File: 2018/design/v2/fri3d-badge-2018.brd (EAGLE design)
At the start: 80 x 60 mm, 1 part

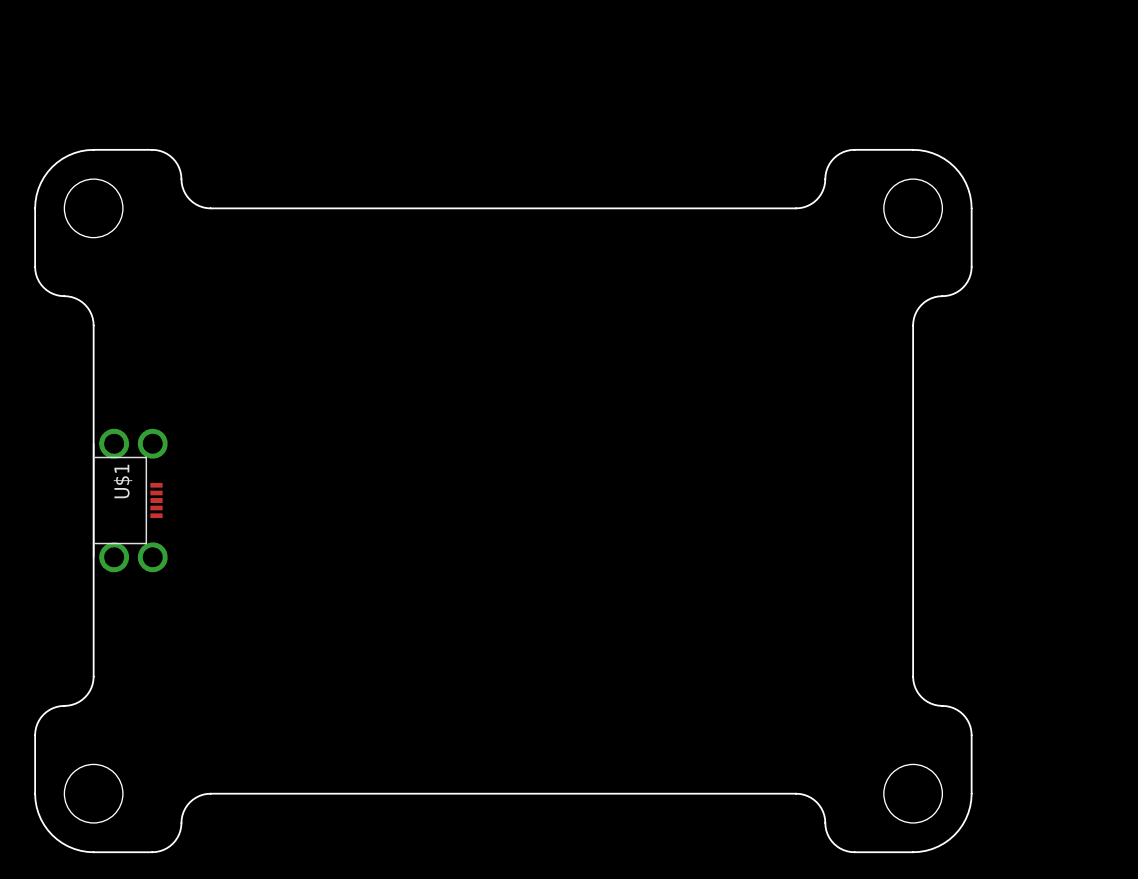
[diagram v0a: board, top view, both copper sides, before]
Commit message: completed draft of schematic for prototype 2
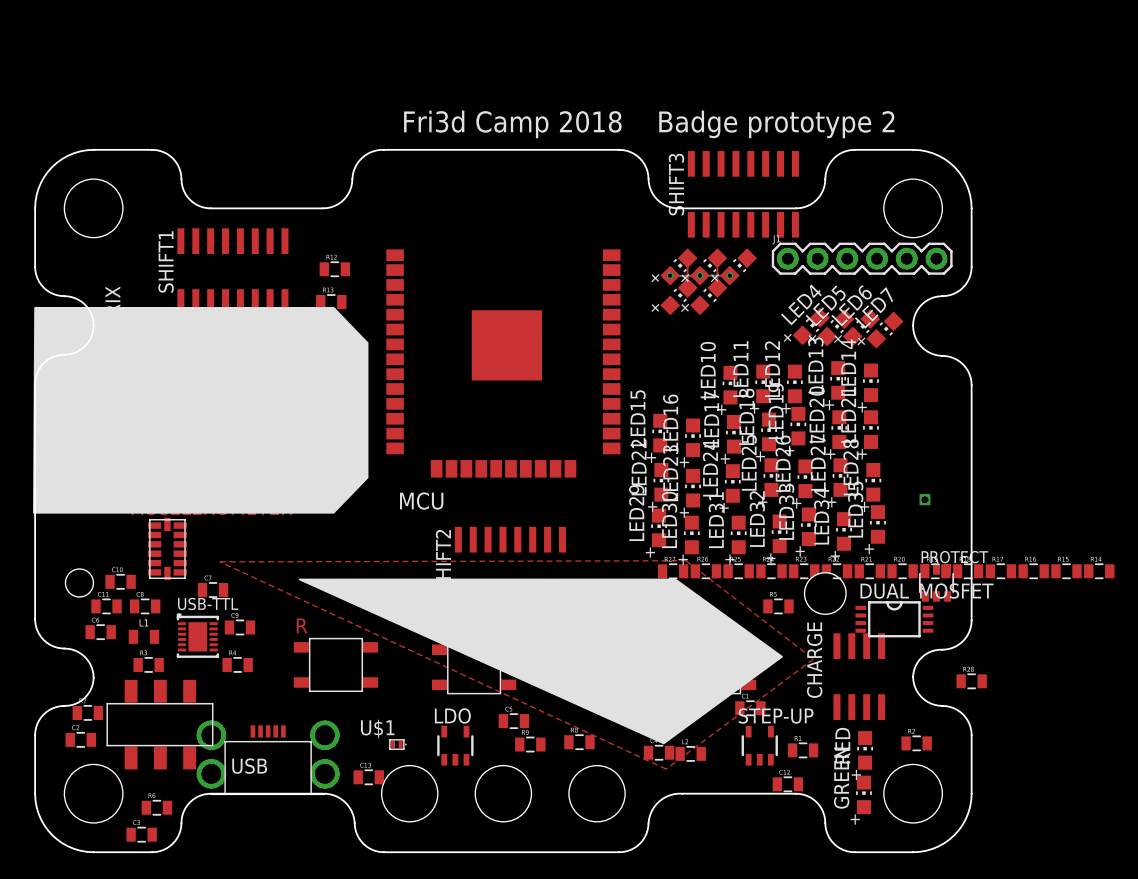
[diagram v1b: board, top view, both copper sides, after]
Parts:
- added A, B, D, R: SWITCH-MOMENTARY-4.5MM, switches:SWITCH-MOMENTARY-4.5MM
- added ACCELEROMETER: ADXL345BCCZ, ic:LGA
- added C1, C2: 10uF, passive:0805
- added C10: 4.7uF, passive:0805
- added C11, C3, C9: 0.1uF, passive:0805
- added C12, C13: 22uF, passive:0805
- added C4, C5: 1uF, passive:0805
- added C6, C7: 47pF, passive:0805
- added C8: 0.01uF, passive:0805
- added CHARGE: TP4056, power:SO8
- added DUAL_MOSFET: FS8205A, ic:TSSOP8
- added GREEN, LED1, LED10, LED11, LED12, LED13, LED14, LED15, LED16, LED17, LED18, LED19, LED2, LED20, LED21, LED22, LED23, LED24, LED25, LED26, LED27, LED28, LED29, LED3, LED30, LED31, LED32, LED33, LED34, LED35, LED4, LED5, LED6, LED7, LED8, LED9, RED: (no value), led:CHIP-LED0805
- added J1: (no value), SparkFun-Connectors:1X06
- added L1: (no value), SparkFun-Coils:0805
- added L2: 10uH, passive:0805
- added LDO: XC6210, power:SOT23-5
- added MCU: ESP-WROOM-32, esp32:ESP-WROOM-32
- added PROTECT: DW01-P, power:SOT23-6
- added R1, R2, R7: 1K, passive:0805
- added R10, R11, R8, R9: 10K, passive:0805
- added R12: 82K, passive:0805
- added R13: 11K, passive:0805
- added R14, R15, R16, R17, R18, R19, R20, R21, R22, R23, R24, R25, R26, R27: (no value), passive:0805
- added R28: 0, passive:0805
- added R3, R4: 27, passive:0805
- added R5: 1.2K, passive:0805
- added R6: 100, passive:0805
- added RIGHT_EYE: 5x7 LED DOT MATRIX, led:5X7_DOT_LED_MATRIX
- added SHIFT1, SHIFT2, SHIFT3: 74HC595, ic:SO16
- added STEP-UP: SX1308, power:SOT23-5
- added U$3: CR18650, setup:BATTERY_HOLDER_18650
- added U$7: SLIDE_DPDT, switches:SLIDE_SWITCH
- added USB: USB_MICRO_B, connector:USB_MICRO_B
- added USB-TTL: FT234XD, ftdi-chip:DFN12
- U$1: value USB_MICRO_B -> SCHOTTKY; device connector:USB_MICRO_B -> passive:SOD993
- moved U$1 29.3 mm to (30.9, 9.20), turned to 0 degrees
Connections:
- new net 3V3: A.P$3, A.P$4, ACCELEROMETER.1, ACCELEROMETER.6, B.P$3, B.P$4, C5.1, LDO.5, MCU.2, R8.2, R9.2, SHIFT1.10, SHIFT1.16, SHIFT2.10, SHIFT2.16, SHIFT3.10, SHIFT3.16
- new net 5V: U$7.P$5
- new net 5V_ENABLE: STEP-UP.4
- new net ACC_ENABLE: ACCELEROMETER.7
- new net ACC_INT1: ACCELEROMETER.8
- new net ACC_INT2: ACCELEROMETER.9
- new net ACC_MISO: ACCELEROMETER.12
- new net ACC_MOSI: ACCELEROMETER.13
- new net ACC_SCK: ACCELEROMETER.14
- new net BUTTON-A: B.P$1, B.P$2, R10.2
- new net BUTTON-B: A.P$1, A.P$2, R11.2
- new net D+: C6.1, R4.1, USB.D+
- new net D-: C7.1, R3.1, USB.D-
- new net DOWNLOAD: D.P$1, D.P$2, MCU.25, R9.1
- new net GND: ACCELEROMETER.2, ACCELEROMETER.4, ACCELEROMETER.5, C1.2, C10.2, C11.2, C12.2, C13.2, C2.2, C4.2, C5.2, C6.2, C7.2, C8.2, C9.2, CHARGE.1, CHARGE.3, D.P$3, D.P$4, DUAL_MOSFET.6, DUAL_MOSFET.7, J1.1, LDO.2, MCU.1, MCU.15, MCU.38, MCU.GND, R.P$3, R.P$4, R10.1, R11.1, R13.1, R28.1, R5.1, R7.2, SHIFT1.8, SHIFT2.8, SHIFT3.8, STEP-UP.2, USB-TTL.13, USB-TTL.5, USB.GND, USB.P$6, USB.P$7, USB.P$8, USB.P$9
- new net LC1: R14.1
- new net LC2: R15.1
- new net LC3: R16.1
- new net LC4: R17.1
- new net LC5: R18.1
- new net LC6: R19.1
- new net LC7: R20.1
- new net LEDS_ENABLE: SHIFT1.13, SHIFT2.13, SHIFT3.13
- new net LEDS_RCK: SHIFT1.12, SHIFT2.12, SHIFT3.12
- new net LEDS_SCK: SHIFT1.11, SHIFT2.11, SHIFT3.11
- new net LEDS_SIN: SHIFT1.14
- new net LR1: LED1.A, LED2.A, LED3.A, LED4.A, LED5.A, LED6.A, LED7.A
- new net LR2: LED10.A, LED11.A, LED12.A, LED13.A, LED14.A, LED8.A, LED9.A
- new net LR3: LED15.A, LED16.A, LED17.A, LED18.A, LED19.A, LED20.A, LED21.A
- new net LR4: LED22.A, LED23.A, LED24.A, LED25.A, LED26.A, LED27.A, LED28.A
- new net LR5: LED29.A, LED30.A, LED31.A, LED32.A, LED33.A, LED34.A, LED35.A
- new net N$10: CHARGE.2, R5.2
- new net N$11: C3.2, DUAL_MOSFET.2, DUAL_MOSFET.3, PROTECT.6, R28.2, U$3.-
- new net N$12: PROTECT.2, R7.1
- new net N$13: C3.1, PROTECT.5, R6.2
- new net N$14: DUAL_MOSFET.4, PROTECT.1
- new net N$15: DUAL_MOSFET.5, PROTECT.3
- new net N$18: R12.1, R13.2, STEP-UP.3
- new net N$19: L2.2, STEP-UP.1, U$1.P$1
- new net N$20: SHIFT1.9, SHIFT2.14
- new net N$21: SHIFT2.9, SHIFT3.14
- new net N$22: SHIFT1.7
- new net N$23: SHIFT1.6
- new net N$24: SHIFT1.5
- new net N$25: SHIFT1.4
- new net N$26: SHIFT1.15
- new net N$27: SHIFT1.1
- new net N$28: SHIFT1.2
- new net N$29: SHIFT1.3
- new net N$3: R3.2, USB-TTL.1
- new net N$30: R21.1, RIGHT_EYE.11
- new net N$31: R22.1, RIGHT_EYE.12
- new net N$32: LED1.C, LED15.C, LED22.C, LED29.C, LED8.C, R14.2
- new net N$33: LED16.C, LED2.C, LED23.C, LED30.C, LED9.C, R15.2
- new net N$34: LED10.C, LED17.C, LED24.C, LED3.C, LED31.C, R16.2
- new net N$35: LED11.C, LED18.C, LED25.C, LED32.C, LED4.C, R17.2
- new net N$36: LED12.C, LED19.C, LED26.C, LED33.C, LED5.C, R18.2
- new net N$37: LED13.C, LED20.C, LED27.C, LED34.C, LED6.C, R19.2
- new net N$38: LED14.C, LED21.C, LED28.C, LED35.C, LED7.C, R20.2
- new net N$39: R24.1, RIGHT_EYE.9
- new net N$4: CHARGE.7, R1.1
- new net N$40: R23.1, RIGHT_EYE.2
- new net N$41: R25.1, RIGHT_EYE.4
- new net N$42: R26.1, RIGHT_EYE.5
- new net N$43: R27.1, RIGHT_EYE.6
- new net N$44: SHIFT2.7
- new net N$45: SHIFT2.6
- new net N$46: SHIFT2.5
- new net N$47: SHIFT2.4
- new net N$48: SHIFT2.15
- new net N$49: SHIFT2.1
- new net N$5: R4.2, USB-TTL.12
- new net N$50: SHIFT2.2
- new net N$51: SHIFT2.3
- new net N$52: SHIFT3.7
- new net N$53: SHIFT3.6
- new net N$54: SHIFT3.5
- new net N$55: SHIFT3.4
- new net N$56: SHIFT3.15
- new net N$57: SHIFT3.1
- new net N$58: SHIFT3.2
- new net N$59: SHIFT3.3
- new net N$6: C9.1, USB-TTL.2, USB-TTL.3, USB-TTL.9
- new net N$7: CHARGE.6, R2.1
- new net N$8: R1.2, RED.C
- new net N$9: GREEN.C, R2.2
- new net RC1: R21.2
- new net RC2: R22.2
- new net RC3: R23.2
- new net RC4: R24.2
- new net RC5: R25.2
- new net RC6: R26.2
- new net RC7: R27.2
- new net RESET: MCU.3, R.P$1, R.P$2, R8.1
- new net RR1: RIGHT_EYE.1
- new net RR2: RIGHT_EYE.3
- new net RR3: RIGHT_EYE.10
- new net RR4: RIGHT_EYE.7
- new net RR5: RIGHT_EYE.8
- new net RX: J1.4, MCU.34, USB-TTL.7
- new net TX: J1.5, MCU.35, USB-TTL.10
- new net USB-RAW: C8.1, L1.1, USB.VBUS
- new net VBAT: C1.1, CHARGE.5, R6.1, U$3.+, U$7.P$3
- new net VCC: C12.1, C4.1, L2.1, LDO.1, LDO.3, STEP-UP.5, U$7.P$2
- new net VSTEPUP: C13.1, R12.2, U$1.P$2, U$7.P$4
- new net VUSB: C10.1, C11.1, C2.1, CHARGE.4, CHARGE.8, GREEN.A, L1.2, RED.A, U$7.P$1, U$7.P$6, USB-TTL.4
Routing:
- net LR1: track 0.00 -> 5.11 mm, vias 0 -> 3
- net N$32: track 0.00 -> 2.56 mm
- net N$33: track 0.00 -> 2.56 mm
- added copper zone on layer 1, net N$1
- added copper zone on layer 1, net N$2
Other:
- outline, holes or cut-outs redrawn
- board text added: "Badge prototype 2"
- board text added: "Fri3d Camp 2018"

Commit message: added extension headers + expansion board
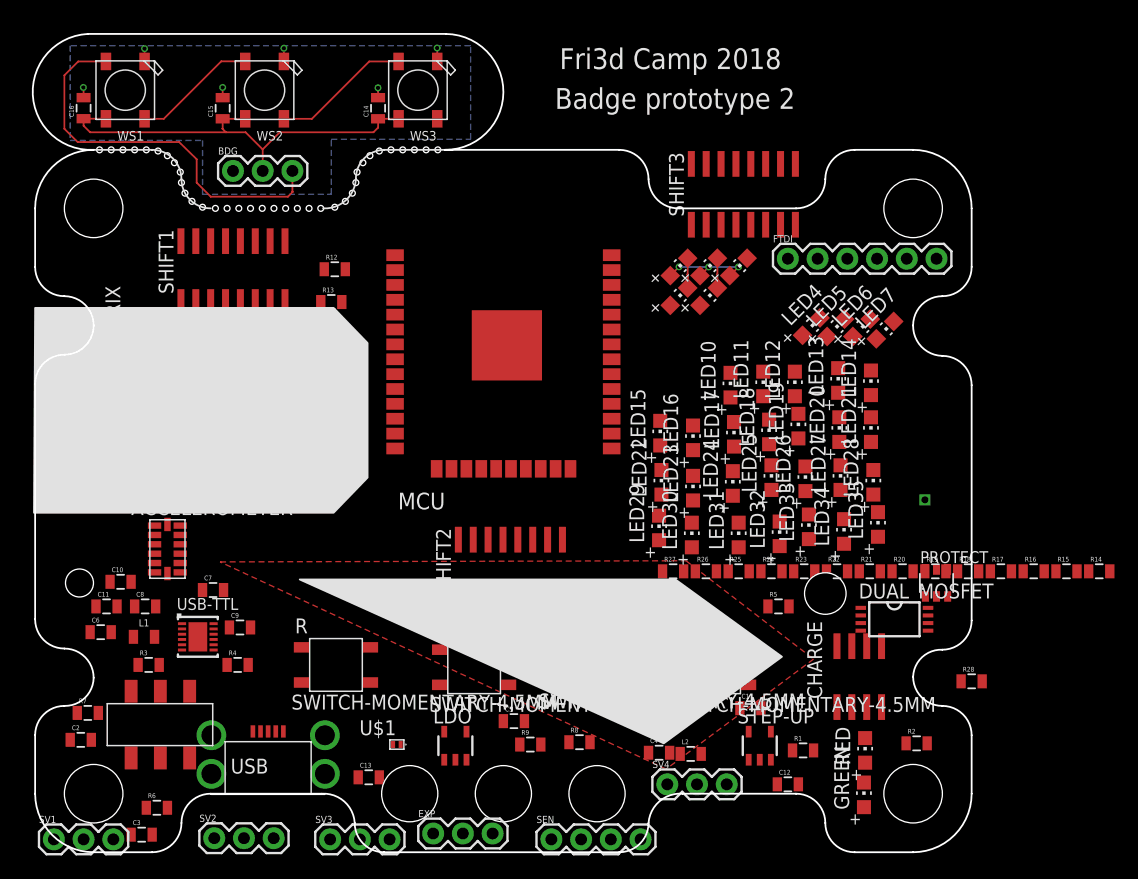
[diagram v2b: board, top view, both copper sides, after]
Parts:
- added BDG, EXP, SV1, SV2, SV3, SV4: (no value), SparkFun-Connectors:1X03
- added C14, C15, C16: 0.1uF, passive:0805
- added SEN: (no value), SparkFun-Connectors:1X04
- added WS1, WS2, WS3: WS2812B5050, adafruit:WS2812B
- renumbered J1 to FTDI, U$7 to PWR
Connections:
- new net ECHO: SEN.2
- new net EXP_3V3: BDG.2, C14.1, C15.1, C16.1, WS1.1-VDD, WS2.1-VDD, WS3.1-VDD
- new net EXP_GND: BDG.1, C14.2, C15.2, C16.2, WS1.3-GND, WS2.3-GND, WS3.3-GND
- new net EXP_IO: EXP.3
- new net N$17: WS1.2-DOUT, WS2.4-DIN
- new net N$60: WS2.2-DOUT, WS3.4-DIN
- new net N$61: BDG.3, WS1.4-DIN
- new net PULSE: SEN.3
- new net SERVO1: SV1.3
- new net SERVO2: SV2.3
- new net SERVO3: SV3.3
- new net SERVO4: SV4.3
- net 3V3: now also A.3, A.4, B.3, B.4, EXP.2; no longer A.P$3, A.P$4, B.P$3, B.P$4
- net 5V: now also SEN.4, SV1.2, SV2.2, SV3.2, SV4.2
- net BUTTON-A: now also B.1, B.2; no longer B.P$1, B.P$2
- net BUTTON-B: now also A.1, A.2; no longer A.P$1, A.P$2
- net DOWNLOAD: now also D.1, D.2; no longer D.P$1, D.P$2
- net GND: now also D.3, D.4, EXP.1, R.3, R.4, SEN.1, SV1.1, SV2.1, SV3.1, SV4.1; no longer D.P$3, D.P$4, R.P$3, R.P$4
- net RESET: now also R.1, R.2; no longer R.P$1, R.P$2
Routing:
- net EXP_3V3: track 0.00 -> 36.9 mm
- net N$61: track 0.00 -> 33.6 mm
- net N$60: track 0.00 -> 11.8 mm
- net N$17: track 0.00 -> 10.6 mm
- net EXP_GND: track 0.00 -> 5.97 mm, vias 0 -> 6
- net LR1: track 5.11 -> 8.23 mm
- added copper zone on layer 16, net EXP_GND
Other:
- board size 80 x 60 mm -> 80.2 x 69.9 mm

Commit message: completed first layout prototype 2
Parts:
- removed ACCELEROMETER: ADXL345BCCZ, ic:LGA
- added ACC: ADXL345BCCZ, ic:LGA
- added C17, C18, C19: 1uF, passive:0805
- added D1: SCHOTTKY, passive:SOD993
- added LDO_MCU: XC6210, power:SOT23-5
- added Q1: (no value), mosfet:SOT23
- added R29: 0, passive:0805
- added R30: 240, passive:0805
- added R31, R32: 10K, passive:0805
- added R33: 1K, passive:0805
- R14, R15, R16, R17, R18, R19, R20, R21, R22, R23, R24, R25, R26, R27: value (none) -> 100
- U$1: value SCHOTTKY -> KLJ-1230; device passive:SOD993 -> sound:KLJ-1230
- moved R7 71.6 mm to (72.3, 35.0)
- moved C3 68.9 mm to (73.4, 26.3)
- moved R21 67.4 mm to (5.30, 37.7), turned to 270 degrees
- moved R22 66.6 mm to (3.30, 37.7), turned to 270 degrees
- moved R6 63.1 mm to (69.4, 26.3)
- moved R23 58.1 mm to (9.27, 37.7), turned to 270 degrees
- moved R24 57.3 mm to (7.30, 37.7), turned to 270 degrees
- moved SV1 55.7 mm to (54.9, 17.3)
- moved R2 51.1 mm to (24.5, 14.8), turned to 90 degrees
- moved RED 50.0 mm to (21.7, 17.3), turned to 270 degrees
- moved CHARGE 47.1 mm to (23.6, 9.60)
- moved GREEN 46.9 mm to (25.6, 17.3), turned to 90 degrees
- moved R5 45.6 mm to (19.6, 8.62)
- moved R13 45.1 mm to (47.8, 7.90), turned to 90 degrees
- moved R12 44.5 mm to (47.8, 11.2), turned to 90 degrees
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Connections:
- removed net EXP_3V3: BDG.2, C14.1, C15.1, C16.1, WS1.1-VDD, WS2.1-VDD, WS3.1-VDD
- removed net N$22: SHIFT1.7
- removed net N$23: SHIFT1.6
- removed net N$24: SHIFT1.5
- removed net N$25: SHIFT1.4
- removed net N$26: SHIFT1.15
- removed net N$27: SHIFT1.1
- removed net N$28: SHIFT1.2
- removed net N$29: SHIFT1.3
- removed net N$44: SHIFT2.7
- removed net N$45: SHIFT2.6
- removed net N$46: SHIFT2.5
- removed net N$47: SHIFT2.4
- removed net N$48: SHIFT2.15
- removed net N$49: SHIFT2.1
- removed net N$50: SHIFT2.2
- removed net N$51: SHIFT2.3
- removed net N$52: SHIFT3.7
- removed net N$53: SHIFT3.6
- removed net N$54: SHIFT3.5
- removed net N$55: SHIFT3.4
- removed net N$56: SHIFT3.15
- removed net N$57: SHIFT3.1
- removed net N$58: SHIFT3.2
- removed net N$59: SHIFT3.3
- new net 3V3_MCU: C18.1, LDO_MCU.5, MCU.2
- new net BUZZER: MCU.16, R30.1
- new net EXP_5V: C14.1, C15.1, C16.1, R29.2, WS1.1-VDD, WS2.1-VDD, WS3.1-VDD
- new net N$11: Q1.1, R30.2, R32.2
- new net N$16: BDG.2, R29.1
- new net N$2: Q1.3, R33.1, U$1.-
- new net N$63: Q1.2, R31.1
- net 3V3: now also ACC.1, ACC.6, R33.2, U$1.+; no longer ACCELEROMETER.1, ACCELEROMETER.6, EXP.2, MCU.2
- net 5V: now also EXP.2, PWR.5; no longer PWR.P$5
- net 5V_ENABLE: now also MCU.22
- net ACC_ENABLE: now also ACC.7, MCU.12; no longer ACCELEROMETER.7
- net ACC_INT1: now also ACC.8, MCU.11; no longer ACCELEROMETER.8
- net ACC_INT2: now also ACC.9, MCU.10; no longer ACCELEROMETER.9
- net ACC_MISO: now also ACC.12, MCU.9; no longer ACCELEROMETER.12
- net ACC_MOSI: now also ACC.13, MCU.8; no longer ACCELEROMETER.13
- net ACC_SCK: now also ACC.14, MCU.7; no longer ACCELEROMETER.14
- net BUTTON-A: now also MCU.26
- net BUTTON-B: now also MCU.14
- net ECHO: now also MCU.29
- net EXP_IO: now also MCU.27
- net GND: now also ACC.2, ACC.4, ACC.5, C17.2, C18.2, C19.1, LDO_MCU.2, R31.2, R32.1; no longer ACCELEROMETER.2, ACCELEROMETER.4, ACCELEROMETER.5
- net LC1: now also SHIFT3.7
- net LC2: now also SHIFT3.6
- net LC3: now also SHIFT3.5
- net LC4: now also SHIFT3.4
- net LC5: now also SHIFT3.3
- net LC6: now also SHIFT3.2
- net LC7: now also SHIFT3.1
- net LEDS_RCK: now also C19.2
- net LEDS_SIN: now also MCU.13
- net LR1: now also SHIFT2.7
- net LR2: now also SHIFT2.6
- net LR3: now also SHIFT2.5
- net LR4: now also SHIFT2.4
- net LR5: now also SHIFT3.15
- net N$19: now also D1.P$1; no longer U$1.P$1
- net PULSE: now also MCU.28
- net RC1: now also SHIFT1.4
- net RC2: now also SHIFT1.3
- net RC3: now also SHIFT1.7
- net RC4: now also SHIFT1.5
- net RC5: now also SHIFT1.2
- net RC6: now also SHIFT1.1
- net RC7: now also SHIFT1.15
- net RR1: now also SHIFT1.6
- net RR2: now also SHIFT2.1
- net RR3: now also SHIFT2.2
- net RR4: now also SHIFT2.15
- net RR5: now also SHIFT2.3
- net SERVO1: now also MCU.23
- net SERVO2: now also MCU.24
- net SERVO3: now also MCU.31
- net SERVO4: now also MCU.30
- net VBAT: now also PWR.3; no longer PWR.P$3
- net VCC: now also C17.1, LDO_MCU.1, LDO_MCU.3, PWR.2; no longer PWR.P$2
- net VSTEPUP: now also D1.P$2, PWR.4; no longer PWR.P$4, U$1.P$2
- net VUSB: now also PWR.1, PWR.8; no longer PWR.P$1, PWR.P$6
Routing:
- net 3V3: track 0.00 -> 243.0 mm, vias 0 -> 3
- net VBAT: track 0.00 -> 94.7 mm, vias 0 -> 3
- net LR2: track 0.00 -> 74.0 mm, vias 0 -> 8
- net LR3: track 0.00 -> 71.7 mm, vias 0 -> 8
- net GND: track 0.00 -> 70.3 mm, vias 0 -> 60
- net LR4: track 0.00 -> 69.8 mm, vias 0 -> 8
- net 5V: track 0.00 -> 69.5 mm
- net LR1: track 8.23 -> 76.2 mm, vias 3 -> 8
- net TX: track 0.00 -> 66.1 mm
- net RX: track 0.00 -> 63.4 mm
- net LEDS_RCK: track 0.00 -> 61.3 mm, vias 0 -> 3
- net VUSB: track 0.00 -> 58.0 mm
- net LEDS_ENABLE: track 0.00 -> 54.4 mm, vias 0 -> 3
- net LEDS_SCK: track 0.00 -> 54.4 mm, vias 0 -> 3
- net VCC: track 0.00 -> 46.7 mm
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- added copper zone on layer 16, net GND
- removed copper zone on layer 1, net N$1
- removed copper zone on layer 1, net N$2
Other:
- outline, holes or cut-outs redrawn
- board text added: "DNF"
